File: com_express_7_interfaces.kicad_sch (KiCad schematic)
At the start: 9 parts, among them J12 Plug_Bus_CE7_EPT_401-51501-51

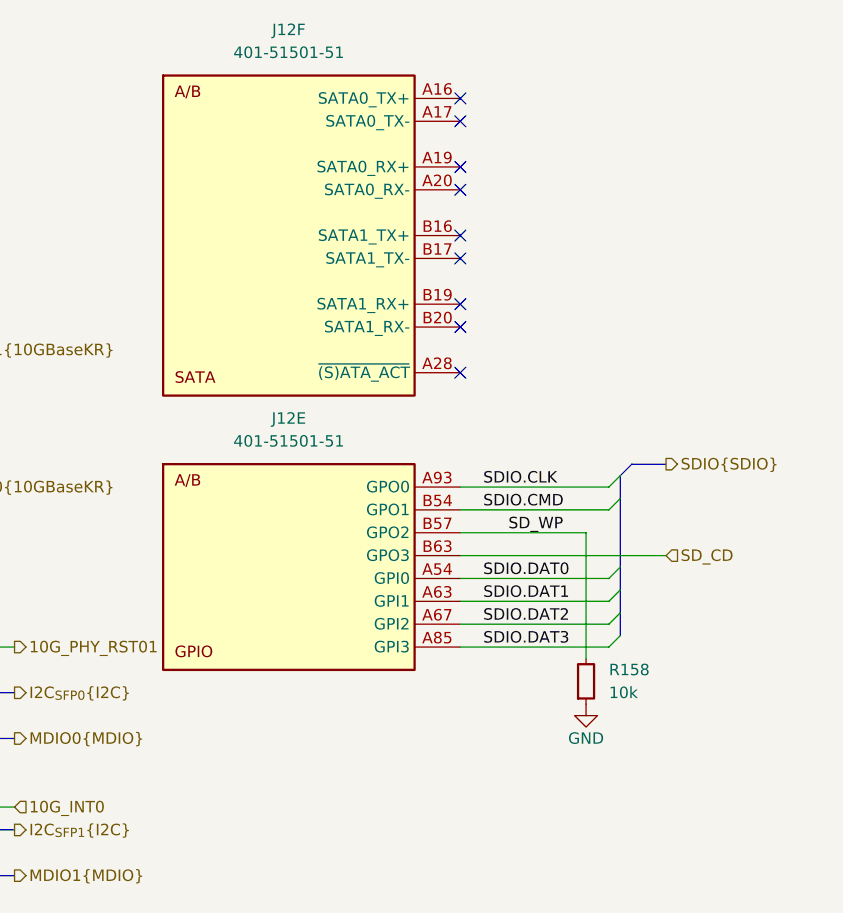
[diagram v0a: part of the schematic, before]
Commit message: [#65447] Fix rotated LEDs, overlapping text and symbols, add rules
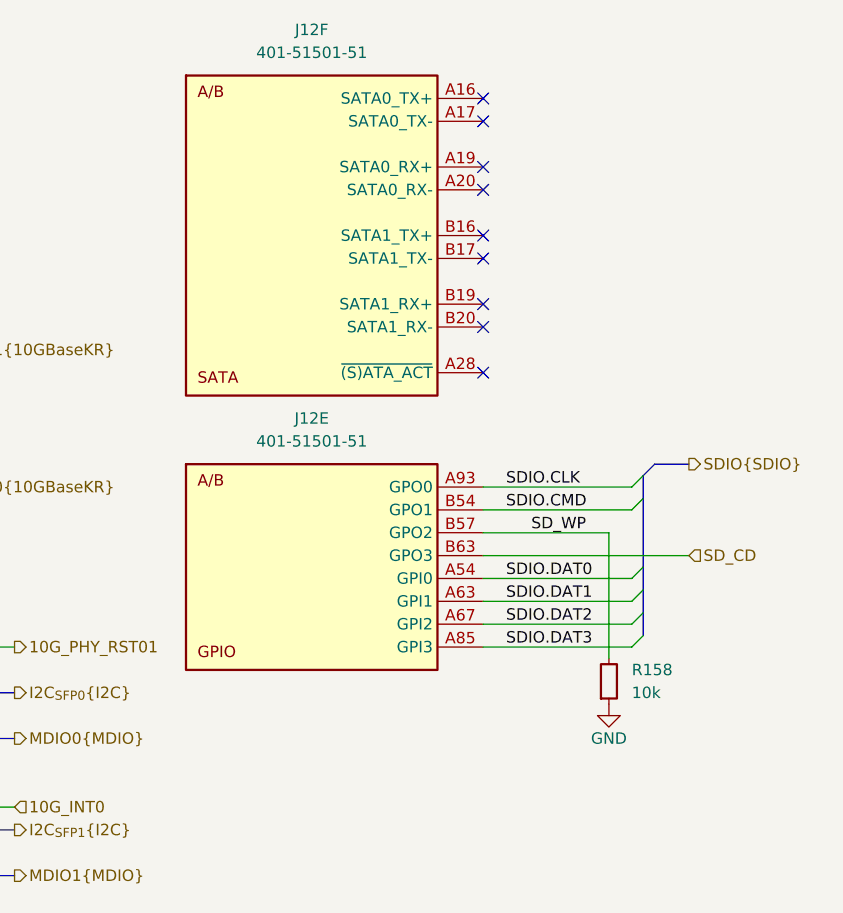
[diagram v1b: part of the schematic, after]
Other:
- moved on the sheet: J12E, J12F, R158

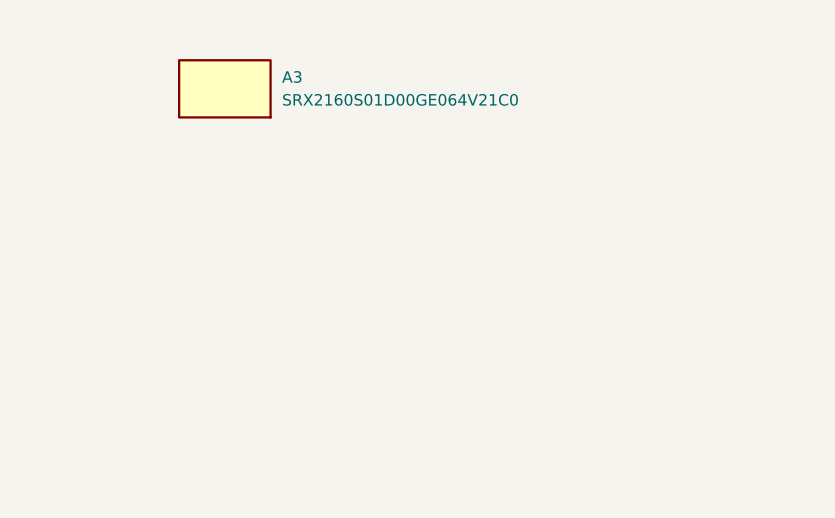
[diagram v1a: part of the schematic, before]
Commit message: [#67758] Add COM mounting standoffs, start rerouting tracks around them
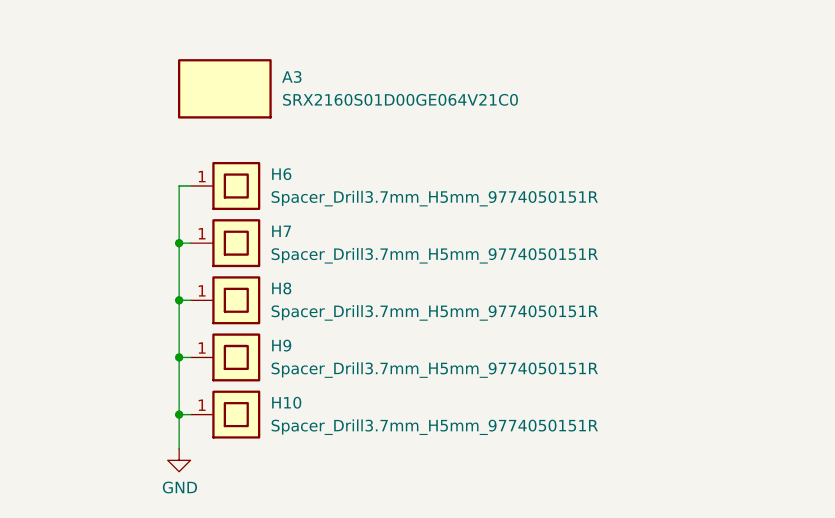
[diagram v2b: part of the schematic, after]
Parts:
- added H10, H6, H7, H8, H9: Spacer_Drill3.7mm_H5mm_9774050151R, antmicro-footprints:Spacer_Drill3.7mm_H5mm_9774050151R, symbol antmicroMechanicalParts:Spacer_Drill3.7mm_H5mm_9774050151R
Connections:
- net GND: now also H10.1, H6.1, H7.1, H8.1, H9.1

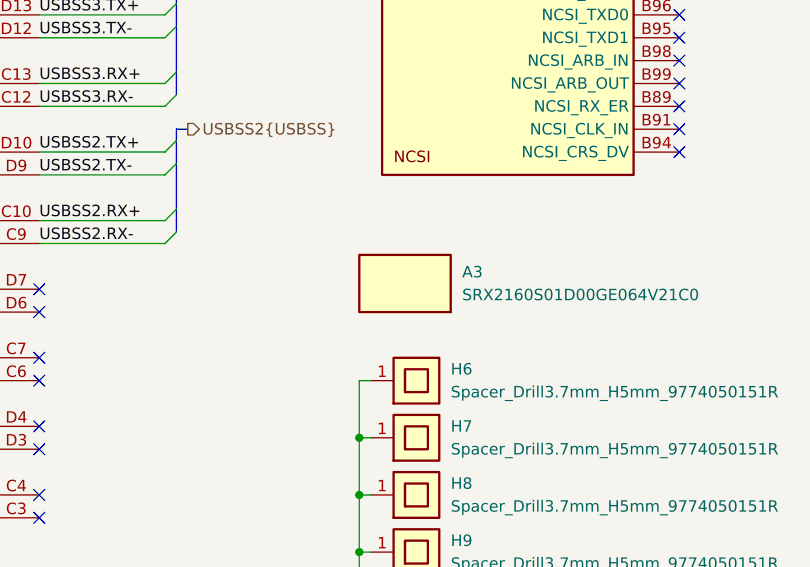
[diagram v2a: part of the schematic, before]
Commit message: [#67758] Mark CE7 mod. DNP; Add more TVS to J4
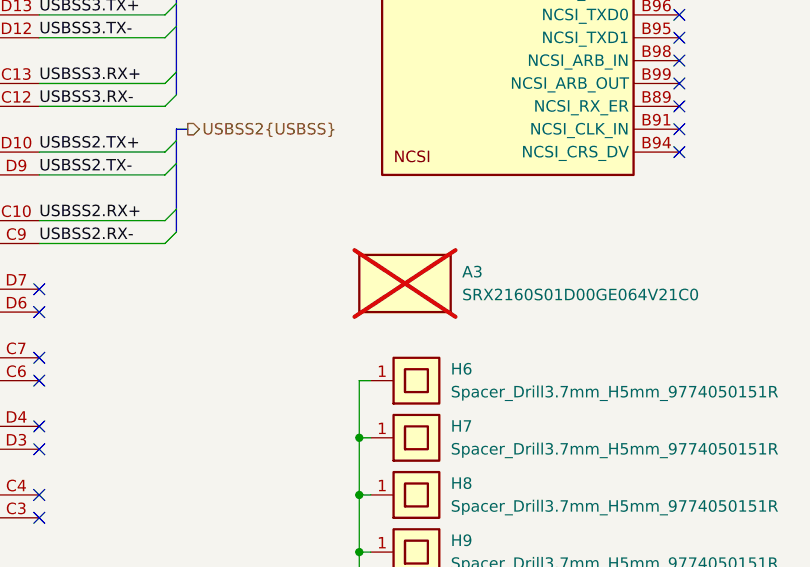
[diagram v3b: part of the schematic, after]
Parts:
- A3: now not fitted
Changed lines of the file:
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@@
   )
   (symbol (lib_id "antmicroModules:Mech_SolidRun_LX2160A-CEX7") (at 246.38 232.41 0) (unit 1)
-    (in_bom no) (on_board yes) (dnp no) (fields_autoplaced)
+    (in_bom no) (on_board yes) (dnp yes) (fields_autoplaced)
     (property "Reference" "A3" (at 257.81 234.315 0)
       (effects (font (size 1.27 1.27) (thickness 0.15)) (justify left))

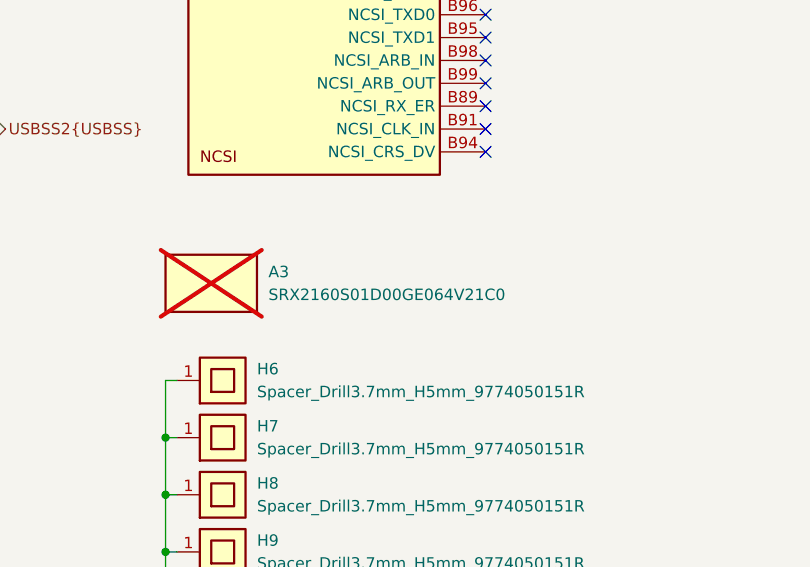
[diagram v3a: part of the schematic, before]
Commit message: [#67758] Update LX2160 from library, clear DRC
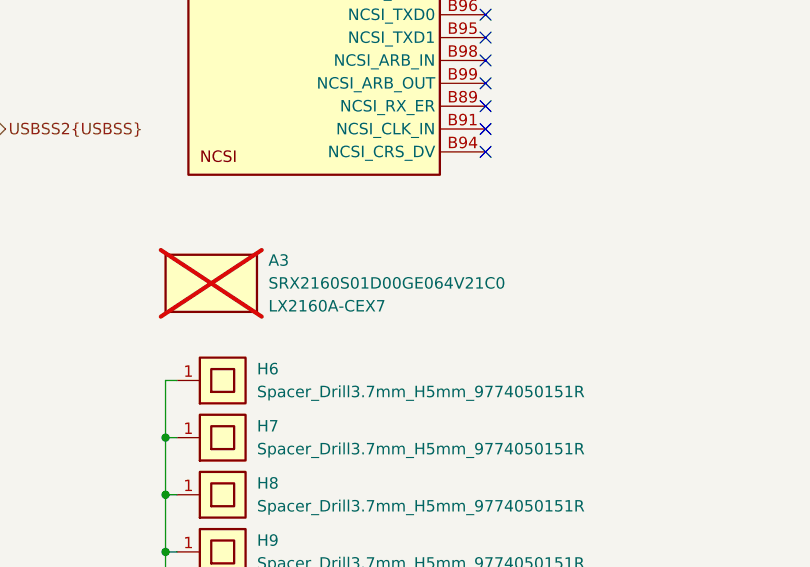
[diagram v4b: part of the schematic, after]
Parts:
- A3: Displayed name (none) -> LX2160A-CEX7
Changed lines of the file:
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@@
   (symbol (lib_id "antmicroModules:Mech_SolidRun_LX2160A-CEX7") (at 246.38 232.41 0) (unit 1)
     (in_bom no) (on_board yes) (dnp yes) (fields_autoplaced)
-    (property "Reference" "A3" (at 257.81 234.315 0)
+    (property "Reference" "A3" (at 257.81 233.045 0)
       (effects (font (size 1.27 1.27) (thickness 0.15)) (justify left))
     )
@@
       (effects (font (size 1.27 1.27) (thickness 0.15)) (justify left bottom) hide)
     )
-    (property "MPN" "SRX2160S01D00GE064V21C0" (at 257.81 236.855 0)
+    (property "MPN" "SRX2160S01D00GE064V21C0" (at 257.81 235.585 0)
       (effects (font (size 1.27 1.27) (thickness 0.15)) (justify left))
     )
@@
       (effects (font (size 1.27 1.27) (thickness 0.15)) (justify left bottom) hide)
     )
+    (property "Displayed name" "LX2160A-CEX7" (at 257.81 238.125 0)
+      (effects (font (size 1.27 1.27)) (justify left))
+    )
     (instances
